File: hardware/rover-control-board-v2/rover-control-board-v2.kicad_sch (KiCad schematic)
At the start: 66 parts, among them J1 XT120, J10 M8 receptacle, J11 Contactor, J2 RET, J3 XT90_REG_OUT, J4 OUT, J5 XT90_REG_RET, J6 CAN1, J7 CAN1, J8 CAN1, J9 M8 receptacle, Q1 PMOS, Q2 CSD19533Q5A, U2 AOZ1284PI, U3 ADS131M08xPBS

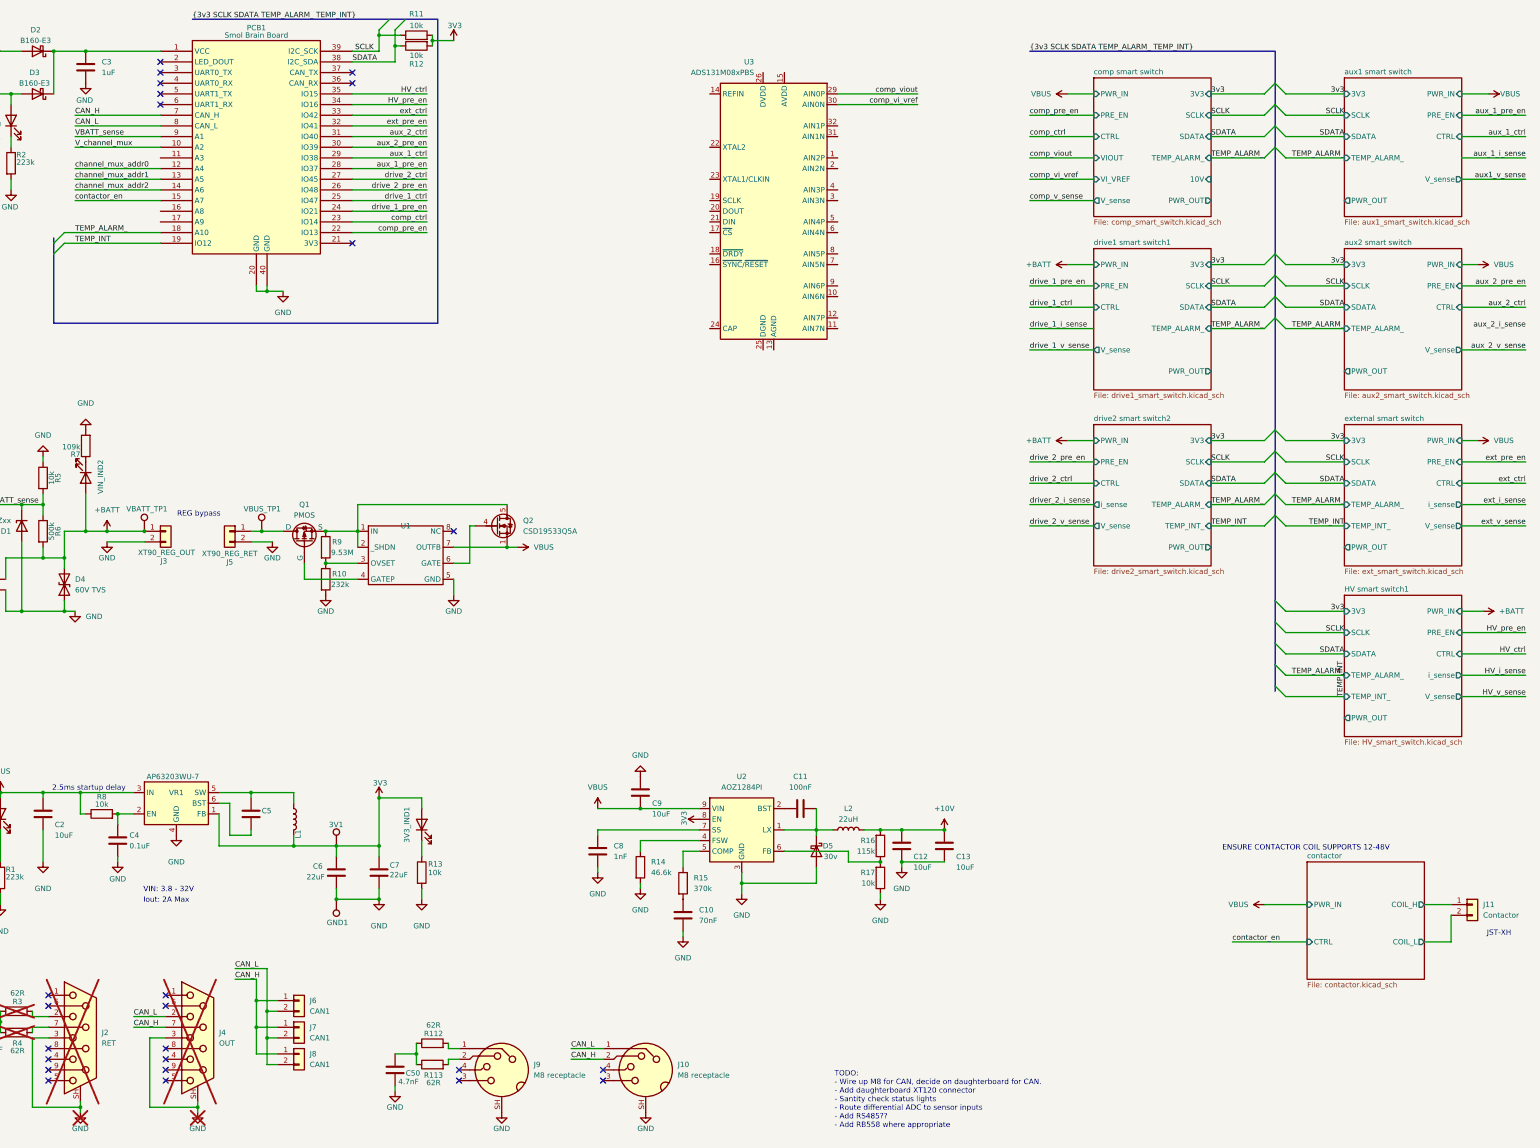
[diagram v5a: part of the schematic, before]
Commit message: Added photovoltaic gate driver and ESD protection
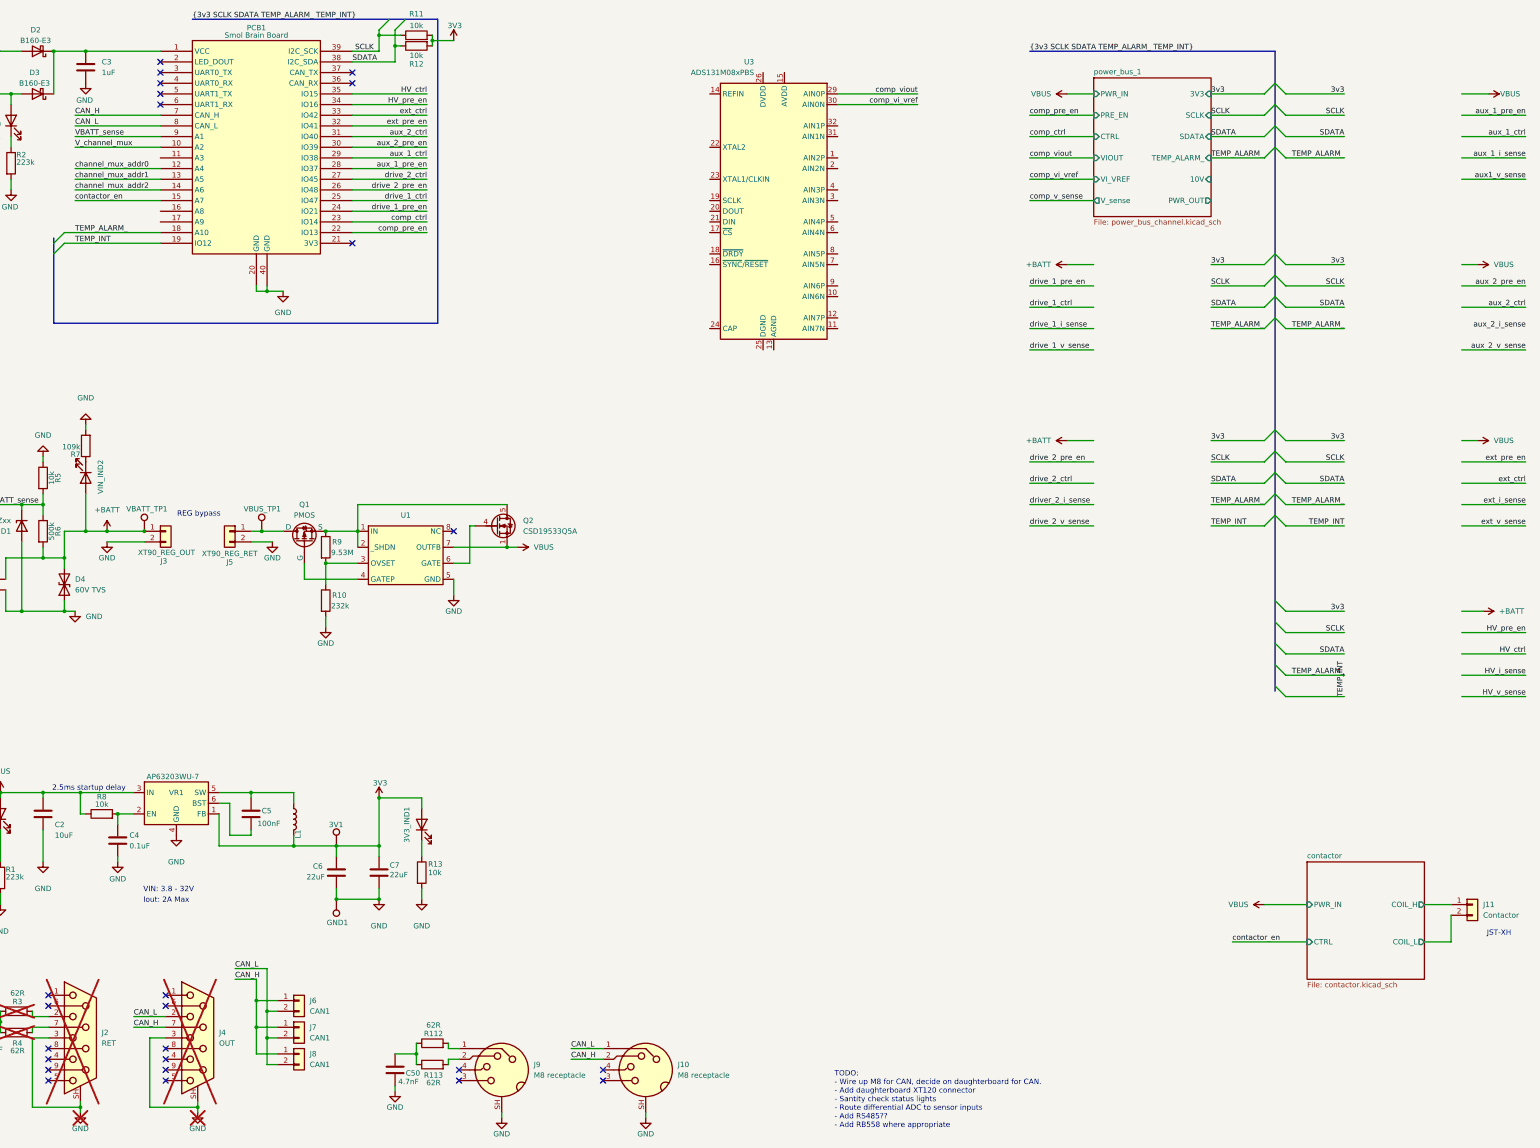
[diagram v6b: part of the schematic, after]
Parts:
- removed C10: 70nF, symbol Device:C
- removed C11: 100nF, symbol Device:C
- removed C12, C13, C9: 10uF, Capacitor_SMD:C_0603_1608Metric, symbol Device:C
- removed C8: 1nF, symbol Device:C
- removed D5: 30v, symbol Device:D_Schottky
- removed L2: 22uH, Inductor_SMD:L_Taiyo-Yuden_MD-4040, symbol Device:L
- removed R14: 46.6k, symbol Device:R
- removed R15: 370k, symbol Device:R
- removed R16: 115k, symbol Device:R
- removed R17: 10k, symbol Device:R
- removed U1: (no value), footprints:max6496, symbol component_library:max6495
- removed U2: AOZ1284PI, Package_SO:SOIC-8-1EP_3.9x4.9mm_P1.27mm_EP2.71x3.7mm, symbol Regulator_Switching:AOZ1284PI
- added U1: (no value), footprints:max6496, symbol component_library:max6496
- C5: value Capacitor 100n 50V 0603 -> 100nF
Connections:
- net GND: now also U1.5 (GND)
- net VBUS: now also U1.7 (OUTFB)
- net at R10.1, R9.2: now also U1.3 (OVSET)
- net at Q1.3 (S), Q2.5 (D), R9.1: now also U1.1 (IN), U1.2 (_SHDN)
- net at Q1.2 (G): now also U1.4 (GATEP)
- net at Q2.4 (G): now also U1.6 (GATE)
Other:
- sheet comp smart switch renamed power_bus_1
- removed sheet HV smart switch1
- removed sheet aux1 smart switch
- removed sheet aux2 smart switch
- removed sheet drive1 smart switch1
- removed sheet drive2 smart switch2
- removed sheet external smart switch
- sheet power_bus_1: file comp_smart_switch.kicad_sch -> power_bus_channel.kicad_sch
- note removed: "ENSURE CONTACTOR COIL SUPPORTS 12-48V"
- moved on the sheet: R10

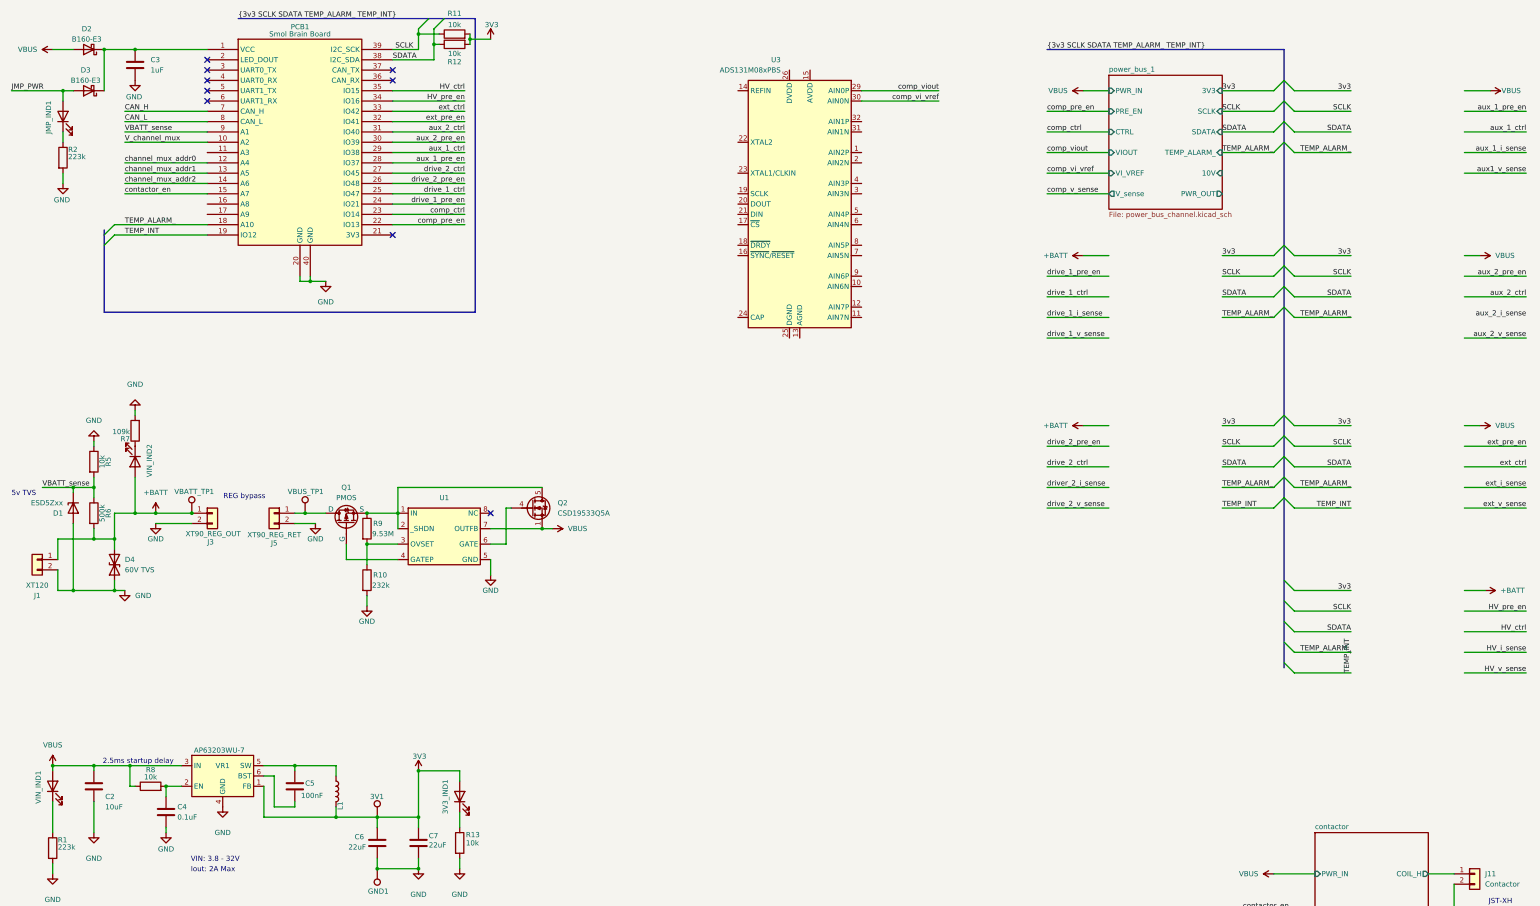
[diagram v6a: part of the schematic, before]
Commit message: footprints and BOM additions
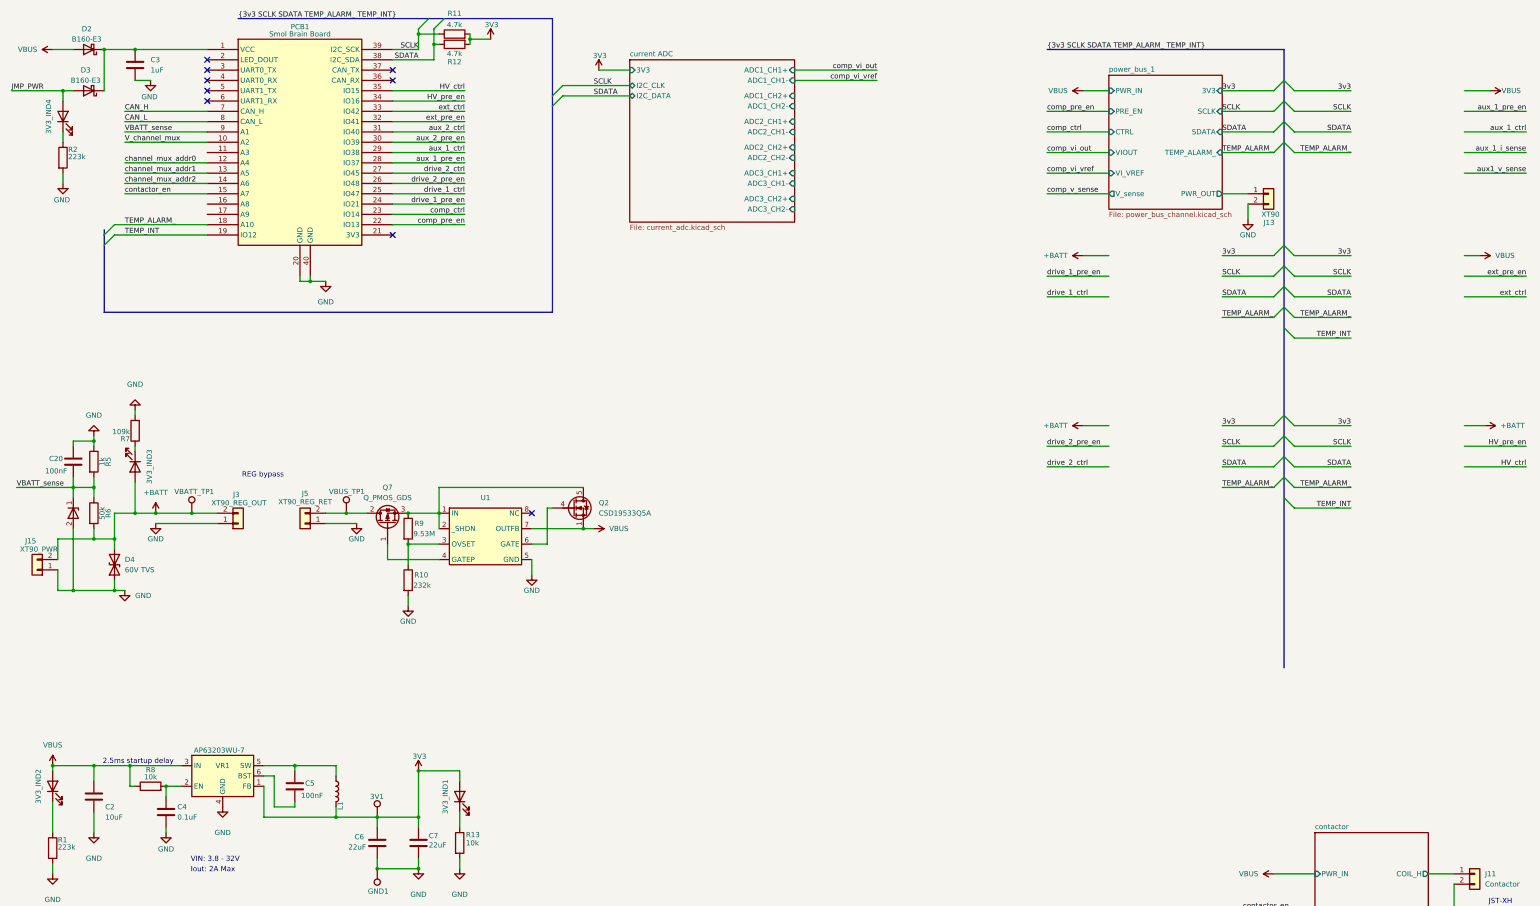
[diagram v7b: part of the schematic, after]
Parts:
- removed D1: ESD5Zxx, Diode_SMD:D_SOD-523, symbol Diode:ESD5Zxx
- removed J1: XT120, symbol Connector_Generic:Conn_01x02
- removed JMP_IND1, VIN_IND1, VIN_IND2: LTST-C190KRKT, LED_SMD:LED_0603_1608Metric, symbol Device:LED
- removed Q1: PMOS, symbol Simulation_SPICE:PMOS
- removed U3: ADS131M08xPBS, Package_QFP:TQFP-32_5x5mm_P0.5mm, symbol Analog_ADC:ADS131M08xPBS
- added 3V3_IND2, 3V3_IND3, 3V3_IND4: 350-599, LED_SMD:LED_0805_2012Metric, symbol Device:LED
- added C20: 100nF, Capacitor_SMD:C_0603_1608Metric, symbol Device:C
- added J13: XT90, footprints:AMASS_XT90-F_1x02_P11.00mm_Vertical, symbol Connector_Generic:Conn_01x02
- added J15: XT90_PWR, footprints:AMASS_XT90-F_1x02_P11.00mm_Vertical, symbol Connector_Generic:Conn_01x02
- added Q7: Q_PMOS_GDS, Package_TO_SOT_SMD:TO-252-2, symbol Transistor_FET:Q_PMOS_GDS
- added U8: (no value), Diode_SMD:D_SOD-882, symbol component_library:PESD3V3V1BLYL
- 3V3_IND1: value LTST-C190KRKT -> 350-599; footprint LED_SMD:LED_0603_1608Metric -> LED_SMD:LED_0805_2012Metric; distributors part number 160-1436-2-ND -> 350-5991180147FCT-ND; manufactuer part number LTST-C190KRKT -> (none); manufacturer Lite-On Inc -> dialight
- C3, C50: footprint (none) -> Capacitor_SMD:C_0603_1608Metric
- D4: footprint (none) -> Diode_SMD:D_SMA; digikey_part_num (none) -> SMAJ54CALFCT-ND
- J10, J9: footprint (none) -> footprints:Tensility_M8_Socket_4P_Shielded_A
- J3, J5: footprint (none) -> footprints:AMASS_XT90-F_1x02_P11.00mm_Vertical
- R10, R112, R113, R9: footprint (none) -> Resistor_SMD:R_0603_1608Metric
- R11, R12: value 10k -> 4.7k; footprint (none) -> Resistor_SMD:R_0603_1608Metric
- R5: value 10k -> 1k; footprint (none) -> Resistor_SMD:R_0603_1608Metric
- R6: value 500k -> 50k; footprint (none) -> Resistor_SMD:R_0603_1608Metric
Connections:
- net +BATT: now also J3.2 (Pin_2), 3V3_IND3.2 (A), J15.2 (Pin_2); no longer J3.1 (Pin_1)
- net GND: now also J3.1 (Pin_1), J5.1 (Pin_1), C20.1, J13.2 (Pin_2), J15.1 (Pin_1), U8.2 (A); no longer J3.2 (Pin_2), J5.2 (Pin_2)
- net JMP_PWR: now also 3V3_IND4.2 (A)
- net VBATT_sense: now also C20.2, U8.1 (K)
- net VBUS: now also 3V3_IND2.2 (A)
- net power_bus_1/PWR_OUT: now also J13.1 (Pin_1)
- net at R7.1: now also 3V3_IND3.1 (K)
- net at R1.1: now also 3V3_IND2.1 (K)
- net at VBUS_TP1.1: now also J5.2 (Pin_2), Q7.2 (D); no longer J5.1 (Pin_1)
- net at Q2.5 (D), R9.1, U1.1 (IN)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: now also Q7.3 (S)
- net at R2.1: now also 3V3_IND4.1 (K)
- net at U1.4 (GATEP): now also Q7.1 (G)
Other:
- added sheet current ADC (current_adc.kicad_sch)
- sheet power_bus_1 ports: added none; removed 10V
- note removed: "5v TVS"
- moved on the sheet: C2, J3, J5, Q2, R10, R9, U1, VBUS_TP1

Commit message: BOM
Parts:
- removed J13: XT90, footprints:AMASS_XT90-F_1x02_P11.00mm_Vertical, symbol Connector_Generic:Conn_01x02
- removed J3: XT90_REG_OUT, footprints:AMASS_XT90-F_1x02_P11.00mm_Vertical, symbol Connector_Generic:Conn_01x02
- removed J5: XT90_REG_RET, footprints:AMASS_XT90-F_1x02_P11.00mm_Vertical, symbol Connector_Generic:Conn_01x02
- added MP1, MP2, MP3: Redcube Press Fit, footprints:MP_Wurth_WP-BUFU_7461097, symbol component_library:Redcube Press Fit
- added U3: MC74HCT595ADTR2G, Package_SO:TSSOP-16_4.4x5mm_P0.65mm, symbol component_library:MC74HCT595ADTR2G
- 3V3_IND1, 3V3_IND2, 3V3_IND4: digikey_part_num (none) -> 350-5991180147FCT-ND
- C1: footprint (none) -> Capacitor_SMD:C_0603_1608Metric; digikey_part_num (none) -> 1276-CL03B472KASVPNCCT-ND; now fitted
- C2: digikey_part_num (none) -> 399-C0603X103K1RAC3121CT-ND
- C20, C3, C5: digikey_part_num (none) -> 311-1344-1-ND
- C4: value 0.1uF -> 100nF; footprint Capacitor_SMD:C_0402_1005Metric -> Capacitor_SMD:C_0603_1608Metric; digikey_part_num (none) -> 311-1344-1-ND
- C50: digikey_part_num (none) -> 1276-CL03B472KASVPNCCT-ND
- C6, C7: digikey_part_num (none) -> 490-5402-1-ND
- D2, D3: digikey_part_num (none) -> B160-E3/5ATGICT-ND
- J10, J9: Manufacturer URL (none) -> https://www.tensility.com/products/54-00274; digikey_part_num (none) -> 839-54-00274-ND
- J11, J6, J7, J8: digikey_part_num (none) -> 455-B2B-XH-A-ND
- J15: Manufacturer URL (none) -> https://www.lcsc.com/product-detail/C3040689.html
- L1: digikey_part_num (none) -> 4816-HPC4018NF-4R7MCT-ND
- PWR_IND3: renamed from 3V3_IND3; digikey_part_num (none) -> 350-5991180147FCT-ND
- Q2: digikey_part_num (none) -> 296-37479-1-ND
- R1, R2: digikey_part_num (none) -> 2019-RN73H1JTTD2233B25CT-ND
- R11, R12: digikey_part_num (none) -> 311-4.70KHRCT-ND
- R112, R113: digikey_part_num (none) -> RMCF0603FT62R0CT-ND
- R13: digikey_part_num (none) -> 311-10.0KHRCT-ND
- R3, R4: footprint (none) -> Capacitor_SMD:C_0603_1608Metric; digikey_part_num (none) -> RMCF0603FT62R0CT-ND; now fitted
- R5: digikey_part_num (none) -> YAG1237CT-ND
- R6: value 50k -> 20k; digikey_part_num (none) -> 2019-RN73R1JTTD2002B25CT-ND
- R7: digikey_part_num (none) -> 541-TNPW0603109KBEEACT-ND
- R8: footprint Resistor_SMD:R_0402_1005Metric -> Capacitor_SMD:C_0603_1608Metric; digikey_part_num (none) -> 541-10.0KHCT-ND
- U1: value (none) -> max6496; digikey_part_num (none) -> MAX6496ATA+TCT-ND
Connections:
- net +BATT: now also MP1.1
- net power_bus_1/PWR_OUT: now also MP3.1
- net at Q7.2 (D), VBUS_TP1.1: now also MP2.1
- net aux_2_ctrl: no longer names the net of PCB1.31 (IO40)
- net aux_2_pre_en: no longer names the net of PCB1.30 (IO39)
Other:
- note added: "JUMP WILL SEND 48V TO SBB!!! Put inline 10-5v reg"
